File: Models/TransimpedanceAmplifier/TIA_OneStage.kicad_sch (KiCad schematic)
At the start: 2 parts, among them U4 OPA828ID

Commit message: Save progress
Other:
- moved on the sheet: R1
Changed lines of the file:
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@@
 	(symbol
 		(lib_id "Device:R_US")
-		(at 130.81 67.31 0)
+		(at 146.05 66.04 90)
 		(unit 1)
 		(exclude_from_sim no)
@@
 		(fields_autoplaced yes)
 		(property "Reference" "R1"
-			(at 133.35 66.0399 0)
+			(at 146.05 59.69 90)
 			(effects
 				(font
 					(size 1.27 1.27)
 				)
-				(justify left)
 			)
 		)
 		(property "Value" "100M, 5%"
-			(at 133.35 68.5799 0)
+			(at 146.05 62.23 90)
 			(effects
 				(font
 					(size 1.27 1.27)
 				)
-				(justify left)
 			)
 		)
 		(property "Footprint" ""
-			(at 131.826 67.564 90)
+			(at 146.304 65.024 90)
 			(effects
 				(font
@@
 		)
 		(property "Datasheet" "~"
-			(at 130.81 67.31 0)
+			(at 146.05 66.04 0)
 			(effects
 				(font
@@
 		)
 		(property "Description" "Resistor, US symbol"
-			(at 130.81 67.31 0)
+			(at 146.05 66.04 0)
 			(effects
 				(font
@@
 		)
 		(property "Purchase Link" "https://www.digikey.com/en/products/detail/vishay-dale/CRCW0603100MJPEAHR/3232293"
-			(at 130.81 67.31 0)
+			(at 146.05 66.04 0)
 			(effects
 				(font

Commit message: Save progress
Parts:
- added C_feedback: 80-220 fF, symbol Device:C
- R_feedback: renamed from R1; Purchase Link https://www.digikey.com/en/products/detail/vishay-dale/CRCW0603100MJPEAHR/3232293 -> https://www.digikey.com/en/products/detail/vishay-dale/CRCW0805100MJPEAHR/3232302
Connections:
- net Input: now reaches U4.2 ('-IN)
- net Input: now also R_feedback.1, C_feedback.1
- net GND: now reaches U4.3 ('+IN)
- net -15V: now reaches U4.4 (V-)
- net Output: now reaches U4.6 (OUT)
- net Output: now also R_feedback.2, C_feedback.2
- net 15V: now reaches U4.7 (V+)
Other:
- moved on the sheet: R_feedback

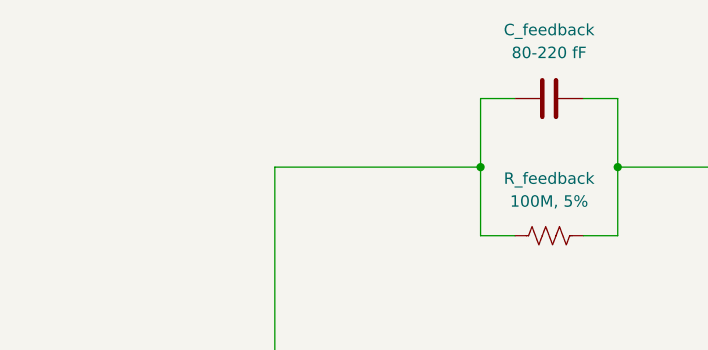
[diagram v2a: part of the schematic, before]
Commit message: Figured out the specific part values for the pole-zero compensation network
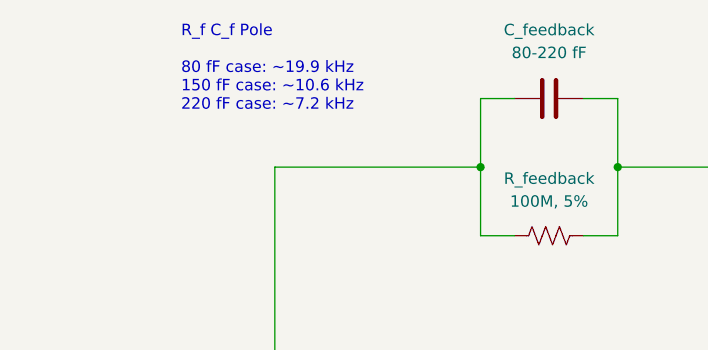
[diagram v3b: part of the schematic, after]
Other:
- note added: "R_f C_f Pole 80 fF case: ~19.9 kHz 150 fF case: ~10.6 kHz 220 fF case: ~7.2 kHz"
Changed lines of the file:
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@@
 	(generator_version "9.0")
 	(paper "A4")
+	(text "R_f C_f Pole\n\n80 fF case: ~19.9 kHz\n150 fF case: ~10.6 kHz\n220 fF case: ~7.2 kHz"
+		(exclude_from_sim no)
+		(at 103.886 42.672 0)
+		(effects
+			(font
+				(size 1.27 1.27)
+			)
+			(justify left top)
+		)
+	)
 	(junction
 		(at 177.8 99.06)

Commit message: All suppliers are out of stock of LM7915L in the simple TO-92-3 package. Resolve this by first tabulating the maximum possible current on each regulator.
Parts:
- U4: Purchase Link (none) -> https://www.digikey.com/en/products/detail/texas-instrument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
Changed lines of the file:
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@@
+			)
+		)
+		(property "Purchase Link" "https://www.digikey.com/en/products/detail/texas-instruments/OPA828IDR/10820196"
+			(at 127 93.98 0)
+			(effects
+				(font
+					(size 1.27 1.27)
+				)
+				(hide yes)
 			)
 		)

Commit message: Refactoring in progress
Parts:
- added C17, C18: 100 nF, 0603, symbol Device:C
- C_feedback: now left out of the parts list
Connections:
- net -15V: now also C17.1
- net 15V: now also C18.2
- net GND: now also C17.2, C18.1

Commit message: Finished for today
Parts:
- C17, C18: Purchase Link (none) -> https://www.digikey.com/en/products/detail/murata-electroni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
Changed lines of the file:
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@@
 			)
 		)
-		(property "Purchase Link" ""
+		(property "Purchase Link" "https://www.digikey.com/en/products/detail/murata-electronics/GRM188R72A104KA35D/702549"
 			(at 172.72 87.63 0)
 			(effects
@@
 			(at 121.92 110.49 0)
 			(effects
+				(font
+					(size 1.27 1.27)
+				)
+				(hide yes)
+			)
+		)
+		(property "Purchase Link" "https://www.digikey.com/en/products/detail/murata-electronics/GRM188R72A104KA35D/702549"
+			(at 121.92 110.49 0)
+			(effects

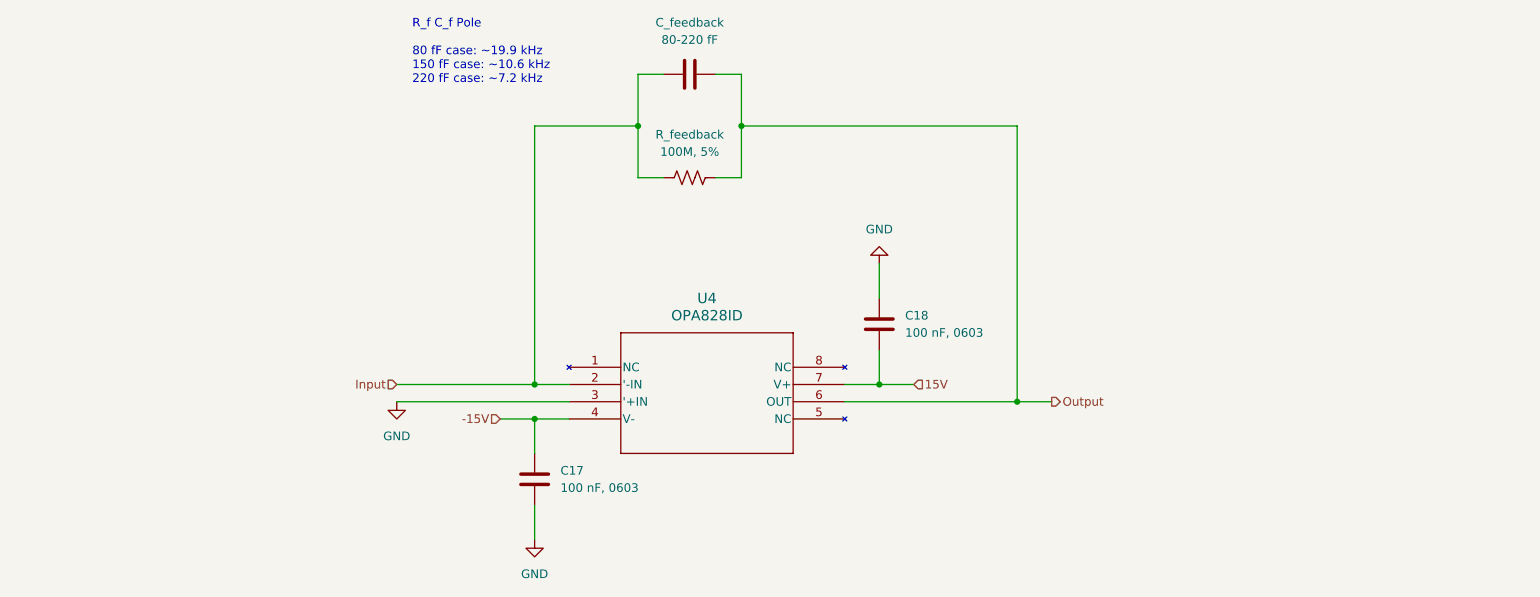
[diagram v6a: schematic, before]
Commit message: This should be all of the pin headers
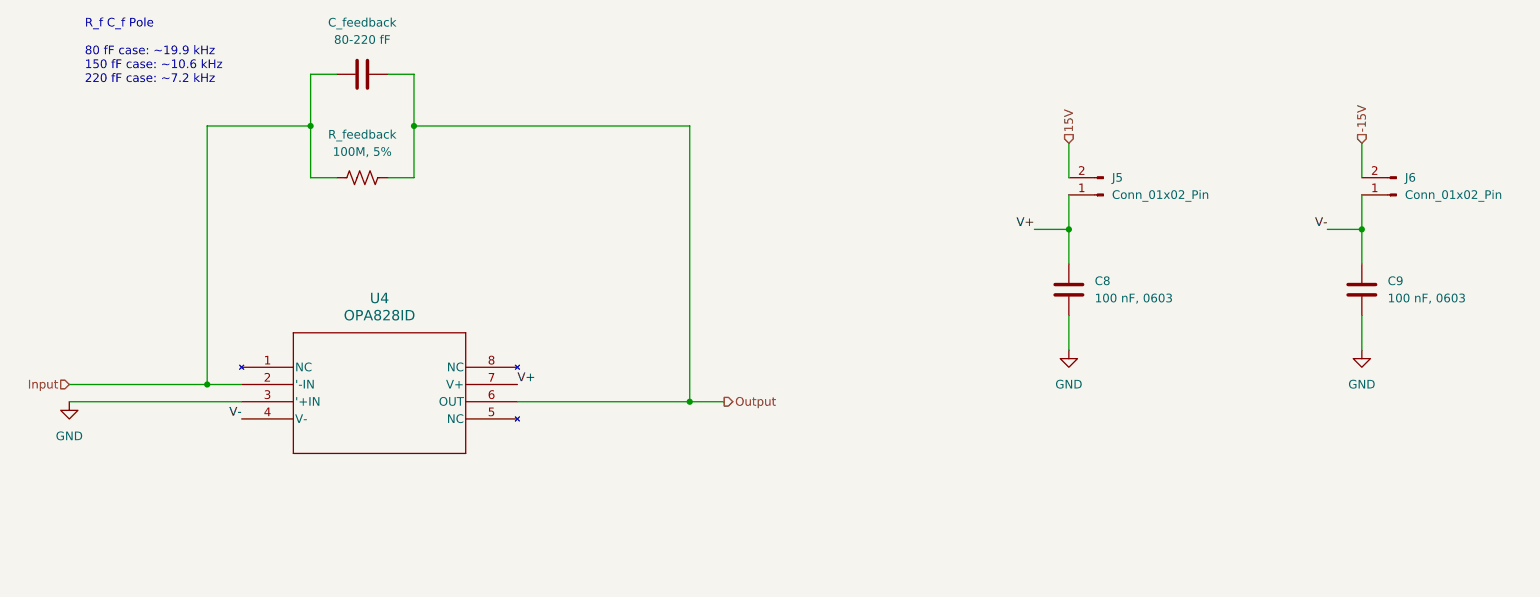
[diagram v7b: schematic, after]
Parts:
- removed C17, C18: 100 nF, 0603, symbol Device:C
- added C8, C9: 100 nF, 0603, symbol Device:C
- added J5, J6: Conn_01x02_Pin, symbol Connector:Conn_01x02_Pin
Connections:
- net -15V: now also J6.2 (Pin_2); no longer U4.4 (V-)
- net 15V: now also J5.2 (Pin_2); no longer U4.7 (V+)
- net GND: now also C8.2, C9.2
- new net V+: C8.1, J5.1 (Pin_1), U4.7 (V+)
- new net V-: C9.1, J6.1 (Pin_1), U4.4 (V-)
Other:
- moved on the sheet: C_feedback, R_feedback, U4

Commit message: Save progress
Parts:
- J5, J6: Purchase Link (none) -> https://www.digikey.com/en/products/detail/sullins-connecto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
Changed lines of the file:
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@@
+			)
+		)
+		(property "Purchase Link" "https://www.digikey.com/en/products/detail/sullins-connector-solutions/QPC02SXGN-RC/2618262"
+			(at 248.92 68.58 0)
+			(effects
+				(font
+					(size 1.27 1.27)
+				)
+				(hide yes)
 			)
 		)
@@
 			(at 205.74 68.58 0)
 			(effects
+				(font
+					(size 1.27 1.27)
+				)
+				(hide yes)
+			)
+		)
+		(property "Purchase Link" "https://www.digikey.com/en/products/detail/sullins-connector-solutions/QPC02SXGN-RC/2618262"
+			(at 205.74 68.58 0)
+			(effects
